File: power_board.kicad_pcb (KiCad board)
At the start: 2 copper layers, 86.1 x 56.4 mm, 18 parts, among them J1 STANDBY SWITCH, J2 TRANSFORMER IN, J3 BIAS OUT, J4 HEATER

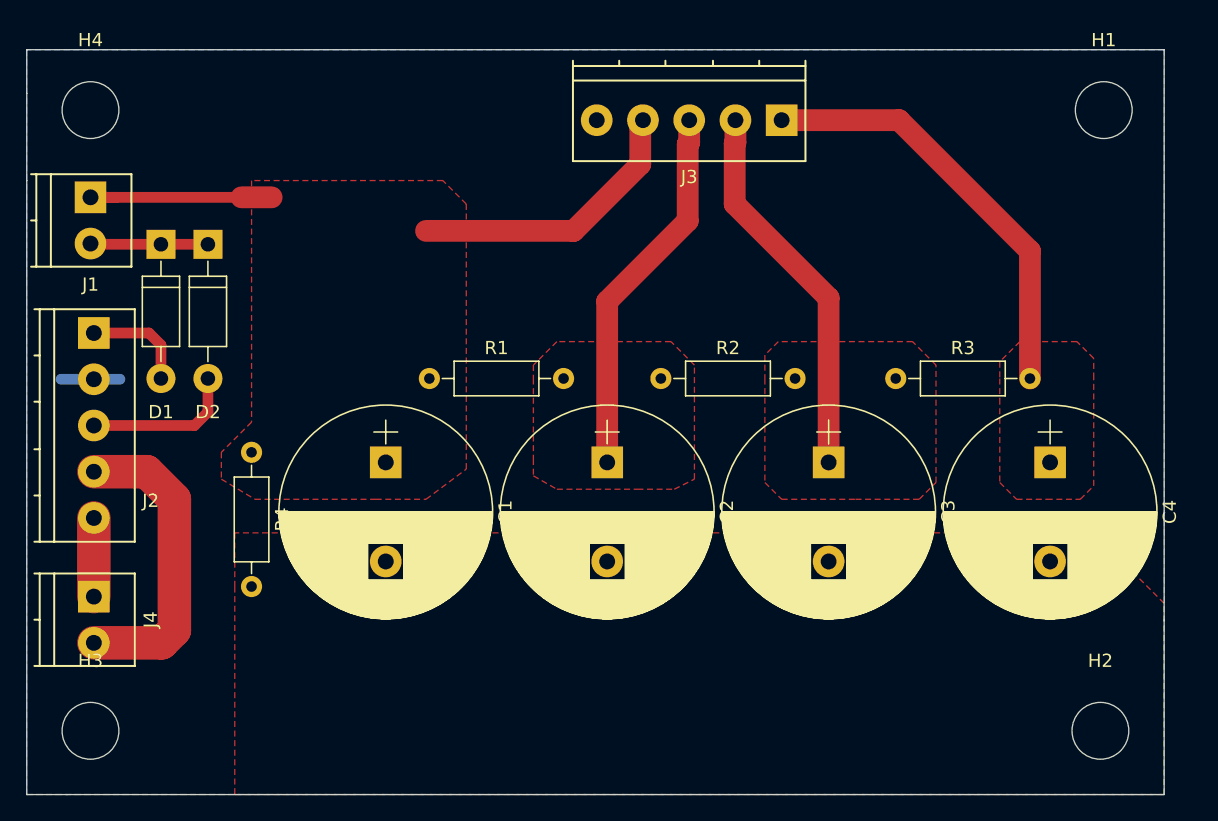
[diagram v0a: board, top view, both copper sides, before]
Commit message: rev 0.2 updates
corrected component pitch issue on connectors for BOM, made power pcb
single sided routing, added aux origin for gerber
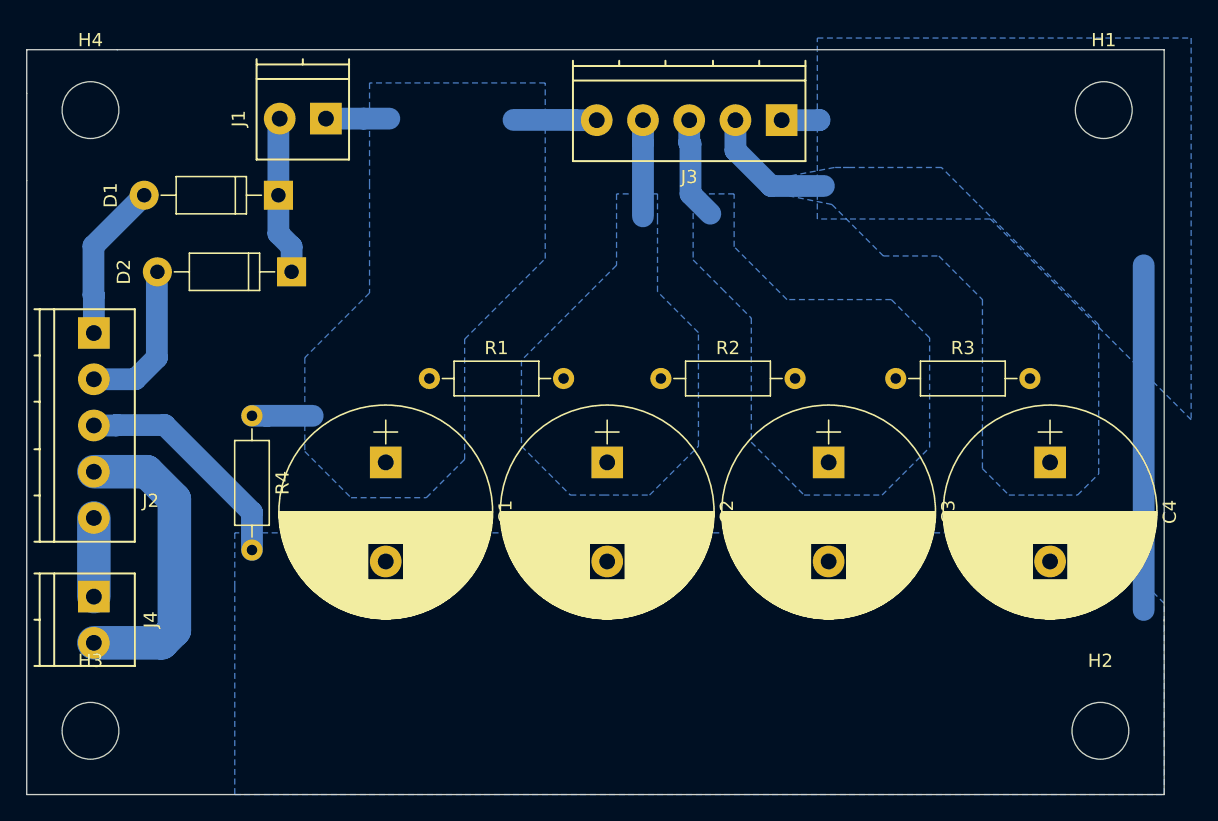
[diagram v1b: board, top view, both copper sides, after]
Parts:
- moved J1 18.8 mm to (117.9, 67.7), turned to 180 degrees
- moved D1 9.64 mm to (114.3, 73.5), turned to 180 degrees
- moved D2 6.67 mm to (115.3, 79.3), turned to 180 degrees
- moved R4 2.76 mm to (112.3, 90.2)
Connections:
- J2 pad 2: GNDA -> /AC_N
- J2 pad 3: /AC_N -> GNDA
- J3 pad 1: /B+3 -> GNDA
- J3 pad 2: /B+2 -> /B+3
- J3 pad 3: /B+1 -> /B+2
- J3 pad 4: /B+ -> /B+1
- J3 pad 5: GNDA -> /B+
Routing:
- net GNDA: track 4.46 -> 46.5 mm
- net /B+3: track 32.6 -> 10.1 mm
- net /B+: track 37.5 -> 15.7 mm
- net /B+1: track 28.5 -> 7.28 mm
- net /B+2: track 28.9 -> 7.74 mm
- net /AC_P: track 7.99 -> 12.0 mm
- net /RECT: track 8.91 -> 12.1 mm
- added copper zone on B.Cu, net /B+
- added copper zone on B.Cu, net /B+1
- added copper zone on B.Cu, net /B+2
- added copper zone on B.Cu, net /B+3
- removed copper zone on F.Cu, net /B+
- removed copper zone on F.Cu, net /B+1
- removed copper zone on F.Cu, net /B+2
- removed copper zone on F.Cu, net /B+3
- removed copper zone on F.Cu, net GNDA
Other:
- net class Default: clearance 0.381 -> 0.7
- rule trace_clearance: 0.381 -> 0.7
